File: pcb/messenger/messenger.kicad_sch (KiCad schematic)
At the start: 57 parts, among them J1 USB_C_Receptacle_USB2.0_16P, J2 Battery, J3 Conn_Coaxial, J4 Display Connector, SW1 BOOT, SW2 EN, U10 W25Q128JVS, U14 24AA32AF-I_MS, U17 MAX17048G+T10, U2 ESP32-S3, U4 USBLC6-2SC6, U5 MCP73831-2-OT, U7 TLV76733DRVx, U8 DMG3415U-7, U9 DMG3415U-7, X1 40MHz

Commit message: still dont work
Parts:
- removed R1: 22, Resistor_SMD:R_0603_1608Metric, symbol Device:R_US
- removed R8: 5.1k, Resistor_SMD:R_0603_1608Metric, symbol Device:R_US
- added C29: 10uF, Capacitor_SMD:C_0603_1608Metric, symbol Device:C
- added C30: 22uF, Capacitor_SMD:C_0603_1608Metric, symbol Device:C
- added L2: 22nH, symbol Device:L
- added U15: TLV76733DRVx, Package_SON:WSON-6-1EP_2x2mm_P0.65mm_EP1x1.6mm_ThermalVias, symbol Regulator_Linear:TLV76733DRVx
- C13, C14: value 10pF -> 12pF
- C15: value 2.7pF -> 3.3pF
- C16: value 2.4pF -> 3.3pF
- L3: value 2.4nH -> 2.2nH
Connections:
- net +3V3: now also U17.3 (VDD); no longer ATGM336H1.8 (VCC), C19.1, C20.1, J4.2 (Pin_2), R13.1, U14.8 (VCC), U9.2 (S)
- net GND: now also J4.3 (Pin_3), J4.4 (Pin_4), C29.2, C30.2, U15.3 (GND), U15.5 (GND), U15.7 (PAD)
- net LORA_DIO1: now also U2.22 (XTAL_32K_N); no longer U2.19 (GPIO14)
- net VCC: now also C29.1, U15.6 (IN)
- net XTAL_P: now also L2.1
- net at U2.54 (XTAL_P): now also L2.2
- removed net GPS_ON/OFF: ATGM336H1.5 (ON/OFF), R18.1, U2.22 (XTAL_32K_N)
- new net +3V3_2: ATGM336H1.8 (VCC), C19.1, C20.1, C30.1, J4.2 (Pin_2), R13.1, U14.8 (VCC), U15.1 (OUT), U15.2 (SNS), U9.2 (S)
- new net LDO_EN: R18.1, U15.4 (EN), U2.19 (GPIO14)
- no-connect marks 16 -> 17

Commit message: v0.5 (save before chip redesign)
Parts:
- removed L1: 2n2, Inductor_SMD:L_0402_1005Metric, symbol Device:L
- added C31: 100nF, Capacitor_SMD:C_0402_1005Metric, symbol Device:C
- added L7: 2.0nH, Inductor_SMD:L_0402_1005Metric, symbol Device:L
- C15, C16: value 3.3pF -> 1.8pF
- C21, C6: value 100nF -> 1uF
- C3: value 10uF -> 1uF
- C4: value 100nF -> 10nF
- C5: value 100nF -> 10uF
- C8: footprint Capacitor_SMD:C_0603_1608Metric -> Capacitor_SMD:C_0402_1005Metric
- C9: value 10uF -> 100nF
- L2: footprint (none) -> Inductor_SMD:L_0603_1608Metric
- L3: value 2.2nH -> 2.4nH
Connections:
- net +3V3: now also C7.1, U2.20 (VDD3P3_RTC), U2.46 (VDD3P3_CPU), C31.1, L7.1; no longer C8.1
- net GND: now also C31.2
- new net: C8.1, L7.2, U2.2 (VDD3P3), U2.3 (VDD3P3)
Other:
- moved on the sheet: C7

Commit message: halfway to v0.4
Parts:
- C31, C8: footprint Capacitor_SMD:C_0402_1005Metric -> Capacitor_SMD:C_0603_1608Metric
- L7: footprint Inductor_SMD:L_0402_1005Metric -> Inductor_SMD:L_0603_1608Metric
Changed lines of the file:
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@@
 			)
 		)
-		(property "Footprint" "Capacitor_SMD:C_0402_1005Metric"
+		(property "Footprint" "Capacitor_SMD:C_0603_1608Metric"
 			(at 214.3252 72.39 0)
 			(effects
@@
 			)
 		)
-		(property "Footprint" "Capacitor_SMD:C_0402_1005Metric"
+		(property "Footprint" "Capacitor_SMD:C_0603_1608Metric"
 			(at 201.6252 72.39 0)
 			(effects
@@
 			)
 		)
-		(property "Footprint" "Inductor_SMD:L_0402_1005Metric"
+		(property "Footprint" "Inductor_SMD:L_0603_1608Metric"
 			(at 205.74 64.77 0)
 			(effects

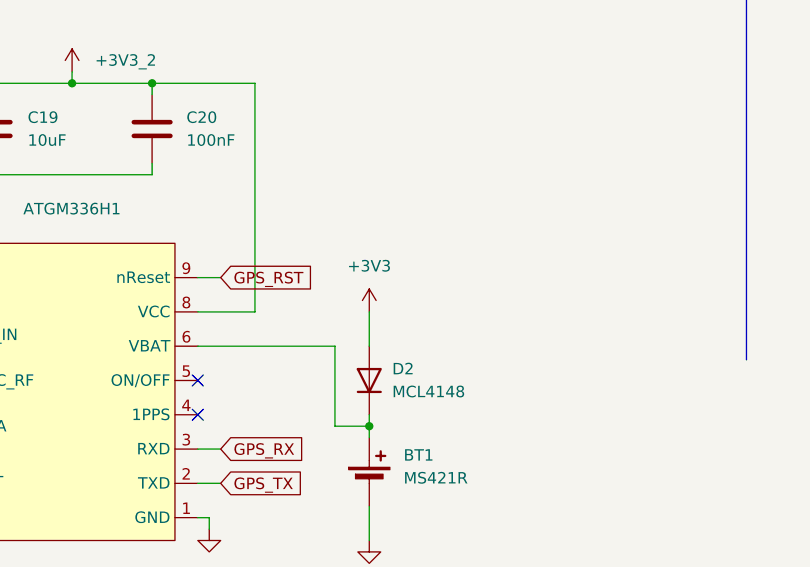
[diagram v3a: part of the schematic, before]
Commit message: Major Revisions v0.4
New decoupling caps, rerouted for better stability. Changed keyboard connector to help longevity of fpc connector.
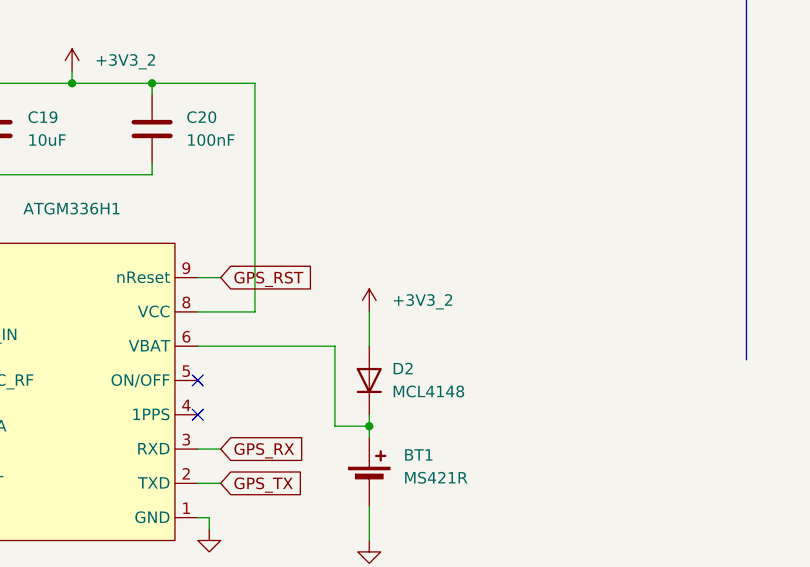
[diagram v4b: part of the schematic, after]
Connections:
- net +3V3: no longer D2.2 (A)
- net +3V3_2: now also D2.2 (A)

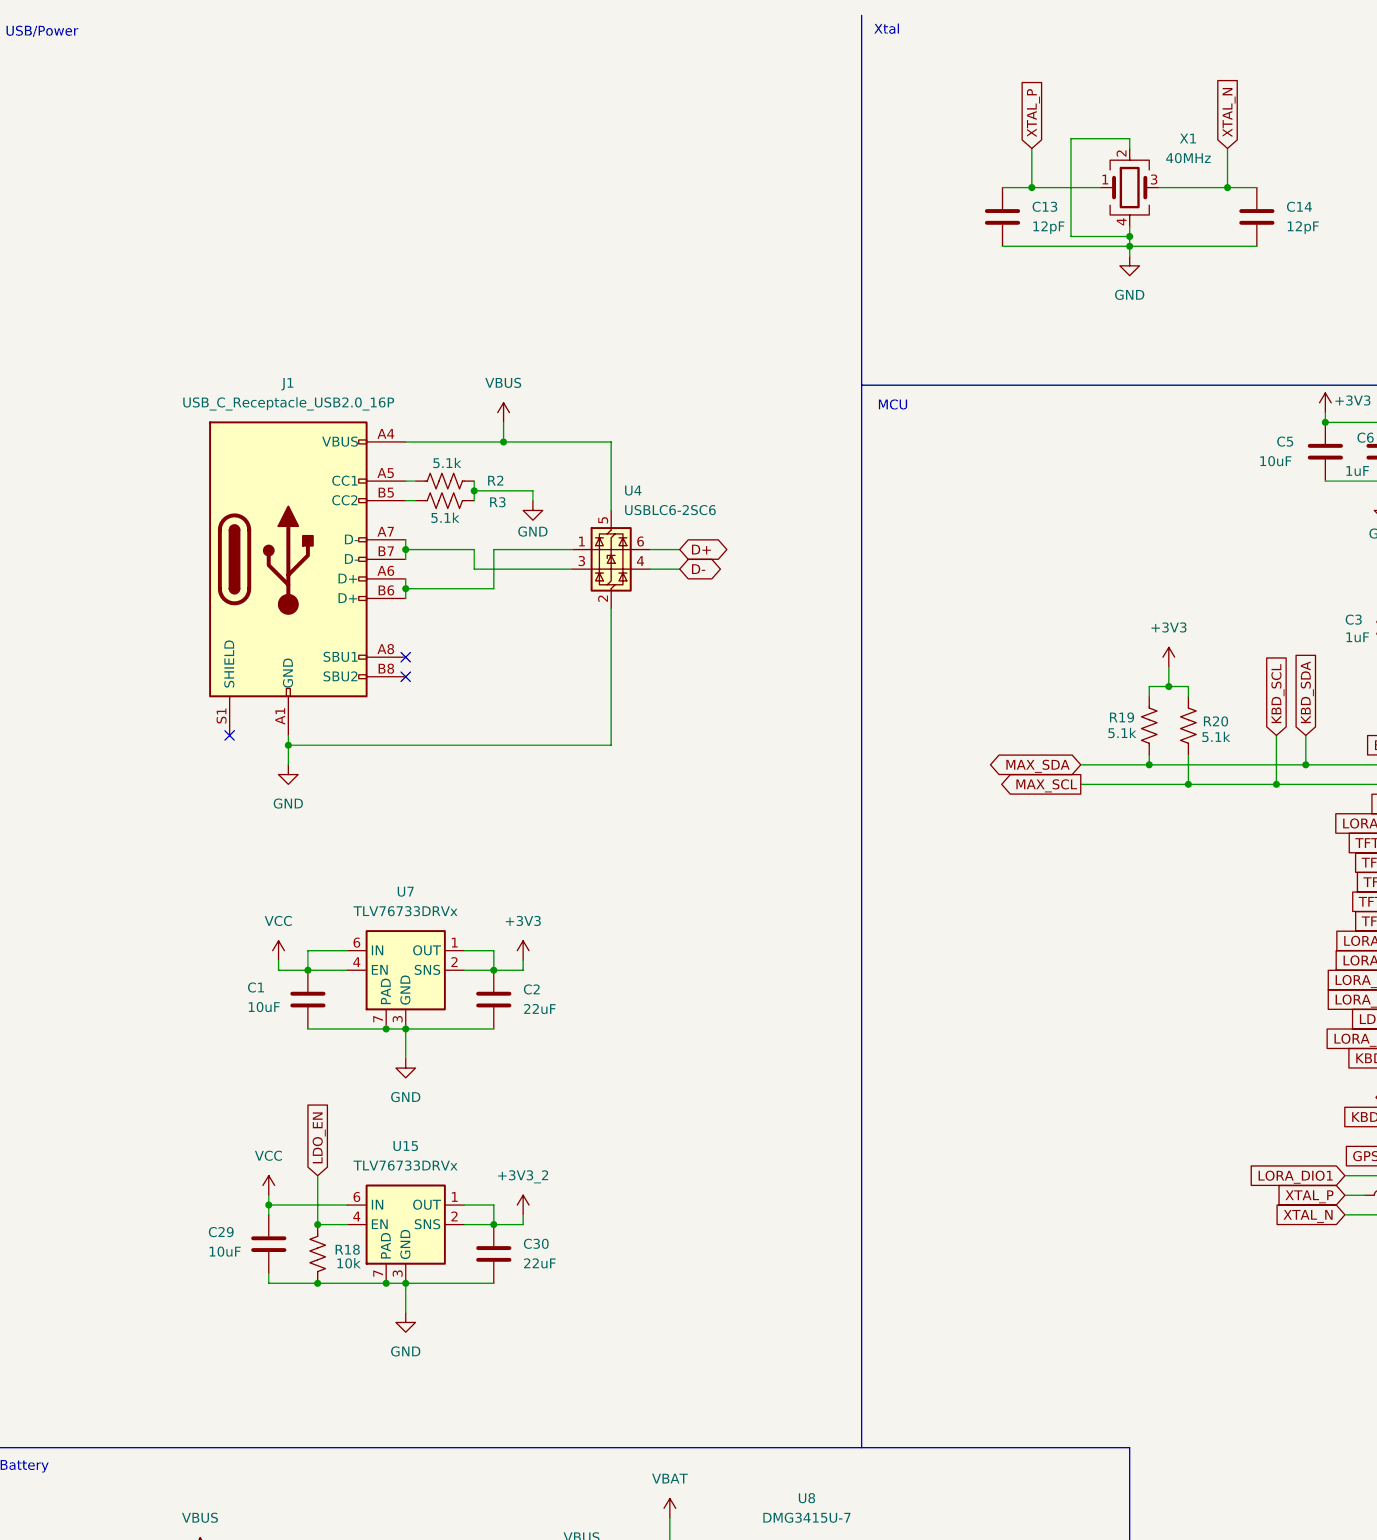
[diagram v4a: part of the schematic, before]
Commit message: v0.4.1 Fixed potential issue with crystal circuitry (PLEASE WORK!!!)
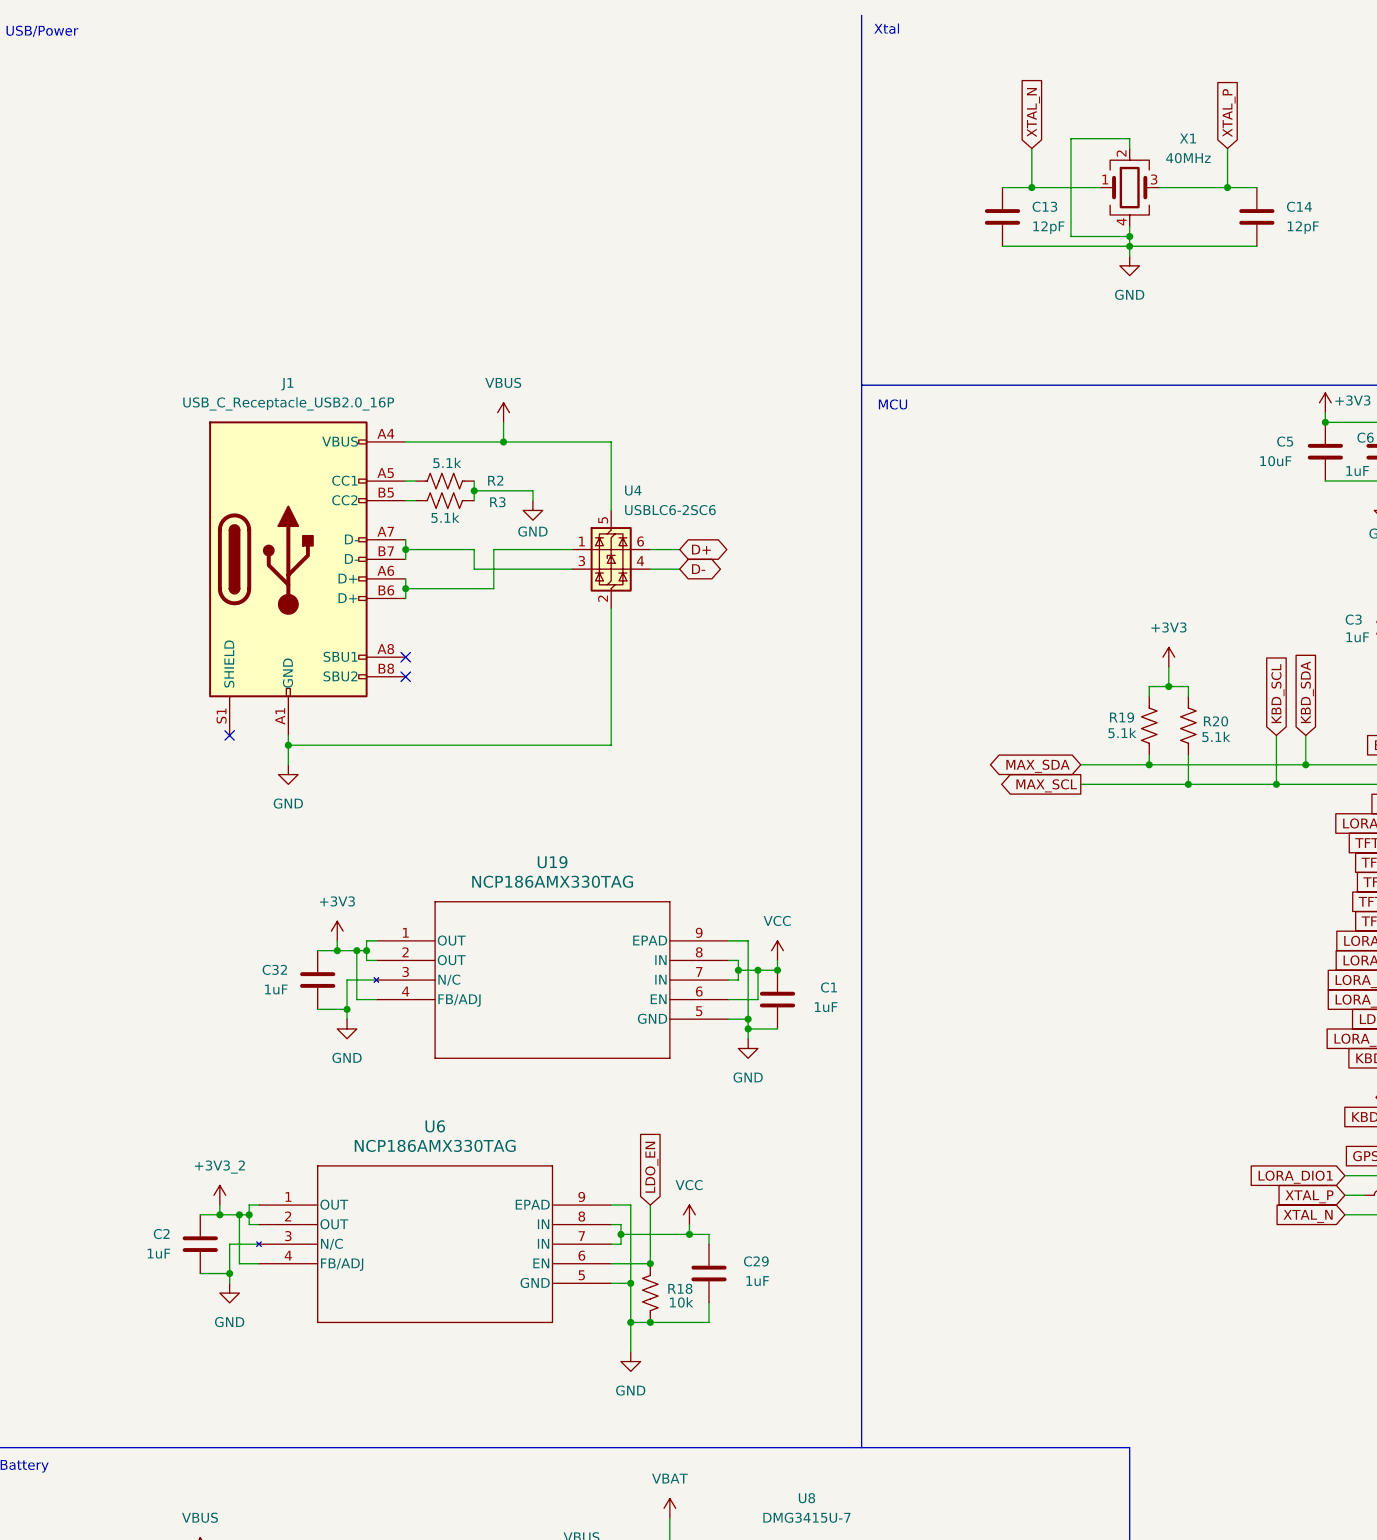
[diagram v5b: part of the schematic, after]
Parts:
- removed C30: 22uF, Capacitor_SMD:C_0603_1608Metric, symbol Device:C
- removed U15, U7: TLV76733DRVx, Package_SON:WSON-6-1EP_2x2mm_P0.65mm_EP1x1.6mm_ThermalVias, symbol Regulator_Linear:TLV76733DRVx
- added C32: 1uF, Capacitor_SMD:C_0603_1608Metric, symbol Device:C
- added U19, U6: NCP186AMX330TAG, NCP186AMX330TAG:XDFN8_1P6X1P2_ONS, symbol NCP186AMX330TAG:NCP186AMX330TAG
- C1, C29: value 10uF -> 1uF
- C2: value 22uF -> 1uF
- C20: footprint Capacitor_SMD:C_0402_1005Metric -> Capacitor_SMD:C_0603_1608Metric
- L2: footprint Inductor_SMD:L_0603_1608Metric -> Inductor_SMD:L_0402_1005Metric
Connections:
- net +3V3: now also C32.1, U19.1 (OUT), U19.2 (OUT), U19.4 (FB/ADJ); no longer C2.1
- net +3V3_2: now also C2.1, U6.1 (OUT), U6.2 (OUT), U6.4 (FB/ADJ)
- net GND: now also C32.2, U19.3 (N/C), U19.5 (GND), U19.9 (EPAD), U6.3 (N/C), U6.5 (GND), U6.9 (EPAD)
- net LDO_EN: now also U6.6 (EN)
- net VCC: now also U19.6 (EN), U19.7 (IN), U19.8 (IN), U6.7 (IN), U6.8 (IN)
- net XTAL_N: now also C13.1, X1.1; no longer C14.1, X1.3
- net XTAL_P: now also C14.1, X1.3; no longer C13.1, X1.1
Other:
- moved on the sheet: R18

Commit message: Version 1.0.0 | Fully working hardware
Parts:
- U17: value MAX17048G+T10 -> MAX17049G+T10
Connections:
- net +3V3: no longer U17.3 (VDD)
- net VBAT: now also U17.3 (VDD)
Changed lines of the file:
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@@
 (kicad_sch
-	(version 20231120)
+	(version 20250114)
 	(generator "eeschema")
-	(generator_version "8.0")
+	(generator_version "9.0")
 	(paper "A3")
+	(text "Display Connector"
+		(exclude_from_sim no)
+		(at 337.566 61.976 0)
+		(effects
+			(font
+				(size 1.27 1.27)
+			)
+		)
+	)
+	(text "MCU"
+		(exclude_from_sim no)
+		(at 129.286 62.738 0)
+		(effects
+			(font
+				(size 1.27 1.27)
+			)
+		)
+	)
+	(text "USB/Power"
+		(exclude_from_sim no)
+		(at 18.796 14.224 0)
+		(effects
+			(font
+				(size 1.27 1.27)
+			)
+		)
+	)
+	(text "LoRa\n"
+		(exclude_from_sim no)
+		(at 331.724 181.102 0)
+		(effects
+			(font
+				(size 1.27 1.27)
+			)
+		)
+	)
+	(text "Battery"
+		(exclude_from_sim no)
+		(at 16.51 200.406 0)
+		(effects
+			(font
+				(size 1.27 1.27)
+			)
+		)
+	)
+	(text "Xtal"
+		(exclude_from_sim no)
+		(at 128.524 13.97 0)
+		(effects
+			(font
+				(size 1.27 1.27)
+			)
+		)
+	)
+	(text "Boot/Reset"
+		(exclude_from_sim no)
+		(at 207.264 13.97 0)
+		(effects
+			(font
+				(size 1.27 1.27)
+			)
+		)
+	)
+	(text "GPS"
+		(exclude_from_sim no)
+		(at 162.4963 213.045 0)
+		(effects
+			(font
+				(size 1.27 1.27)
+			)
+		)
+	)
+	(text "Keyboard"
+		(exclude_from_sim no)
+		(at 333.248 13.97 0)
+		(effects
+			(font
+				(size 1.27 1.27)
+			)
+		)
+	)
 	(junction
 		(at 93.98 170.18)
@@
 	)
 	(junction
+		(at 43.18 260.35)
+		(diameter 0)
+		(color 0 0 0 0)
+	)
+	(junction
 		(at 78.74 67.31)
 		(diameter 0)
@@
 	(wire
 		(pts
+			(xy 43.18 260.35) (xy 46.99 260.35)
+		)
+		(stroke
+			(width 0)
+			(type default)
+		)
+	)
+	(wire
+		(pts
 			(xy 171.45 267.97) (xy 171.45 266.7)
 		)
@@
 	(wire
 		(pts
-			(xy 39.37 260.35) (xy 46.99 260.35)
+			(xy 39.37 260.35) (xy 43.18 260.35)
 		)
 		(stroke
@@
 	(wire
 		(pts
-			(xy 43.18 259.08) (xy 43.18 262.89)
-		)
-		(stroke
-			(width 0)
-			(type default)
-		)
-	)
-	(wire
-		(pts
 			(xy 54.61 133.35) (xy 57.15 133.35)
 		)
@@
 	(wire
 		(pts
+			(xy 43.18 260.35) (xy 43.18 262.89)
+		)
+		(stroke
+			(width 0)
+			(type default)
+		)
+	)
+	(wire
+		(pts
 			(xy 182.88 105.41) (xy 182.88 109.22)
 		)
@@
 		)
 	)
-	(text "Display Connector"
-		(exclude_from_sim no)
-		(at 337.566 61.976 0)
-		(effects
-			(font
-				(size 1.27 1.27)
-			)
-		)
-	)
-	(text "MCU"
-		(exclude_from_sim no)
-		(at 129.286 62.738 0)
-		(effects
-			(font
-				(size 1.27 1.27)
-			)
-		)
-	)
-	(text "USB/Power"
-		(exclude_from_sim no)
-		(at 18.796 14.224 0)
-		(effects
-			(font
-				(size 1.27 1.27)
-			)
-		)
-	)
-	(text "LoRa\n"
-		(exclude_from_sim no)
-		(at 331.724 181.102 0)
-		(effects
-			(font
-				(size 1.27 1.27)
-			)
-		)
-	)
-	(text "Battery"
-		(exclude_from_sim no)
-		(at 16.51 200.406 0)
-		(effects
-			(font
-				(size 1.27 1.27)
-			)
-		)
-	)
-	(text "Xtal"
-		(exclude_from_sim no)
-		(at 128.524 13.97 0)
-		(effects
-			(font
-				(size 1.27 1.27)
-			)
-		)
-	)
-	(text "Boot/Reset"
-		(exclude_from_sim no)
-		(at 207.264 13.97 0)
-		(effects
-			(font
-				(size 1.27 1.27)
-			)
-		)
-	)
-	(text "GPS"
-		(exclude_from_sim no)
-		(at 162.4963 213.045 0)
-		(effects
-			(font
-				(size 1.27 1.27)
-			)
-		)
-	)
-	(text "Keyboard"
-		(exclude_from_sim no)
-		(at 333.248 13.97 0)
-		(effects
-			(font
-				(size 1.27 1.27)
-			)
-		)
-	)
 	(global_label "TFT_D0"
 		(shape input)
@@
 	(symbol
 		(lib_id "power:+3V3")
-		(at 43.18 259.08 0)
-		(unit 1)
-		(exclude_from_sim no)
-		(in_bom yes)
-		(on_board yes)
-		(dnp no)
-		(property "Reference" "#PWR075"
-			(at 43.18 262.89 0)
-			(effects
-				(font
-					(size 1.27 1.27)
-				)
-				(hide yes)
-			)
-		)
-		(property "Value" "+3V3"
-			(at 43.18 255.27 0)
-			(effects
-				(font
-					(size 1.27 1.27)
-				)
-			)
-		)
-		(property "Footprint" ""
-			(at 43.18 259.08 0)
-			(effects
-				(font
-					(size 1.27 1.27)
-				)
-				(hide yes)
-			)
-		)
-		(property "Datasheet" ""
-			(at 43.18 259.08 0)
-			(effects
-				(font
-					(size 1.27 1.27)
-				)
-				(hide yes)
-			)
-		)
-		(property "Description" "Power symbol creates a global label with name \"+3V3\""
-			(at 43.18 259.08 0)
-			(effects
-				(font
-					(size 1.27 1.27)
-				)
-				(hide yes)
-			)
-		)
-		(pin "1"
-		)
-		(instances
-			(project "messenger"
-				(path "/3c3794b6-df2c-4cf7-82cf-83f8f28f2ff8"
-					(reference "#PWR075")
-					(unit 1)
-				)
-			)
-		)
-	)
-	(symbol
-		(lib_id "power:+3V3")
 		(at 232.41 83.82 0)
 		(unit 1)
@@
 			)
 		)
-		(property "Value" "MAX17048G+T10"
+		(property "Value" "MAX17049G+T10"
 			(at 77.47 250.19 0)
 			(effects
@@
 		(at 357.886 22.352)
 		(size 24.384 20.828)
+		(exclude_from_sim no)
+		(in_bom yes)
+		(on_board yes)
+		(dnp no)
 		(fields_autoplaced yes)
 		(stroke
@@
 		(at 355.092 202.692)
 		(size 25.908 21.59)
+		(exclude_from_sim no)
+		(in_bom yes)
+		(on_board yes)
+		(dnp no)
 		(fields_autoplaced yes)
 		(stroke
@@
 		)
 	)
+	(embedded_fonts no)
 )
